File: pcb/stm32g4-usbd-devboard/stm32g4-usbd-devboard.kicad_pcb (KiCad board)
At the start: 2 copper layers, 23.1 x 51.9 mm, 30 parts, among them J1 USB_B_Mini, J2 PIN H 6P, J3 LEFT, J4 RIGHT, U1 USBLC6-2SC6, U2 MCP1700-3302E, U3 STM32G431KBTx, Y1 24MHz

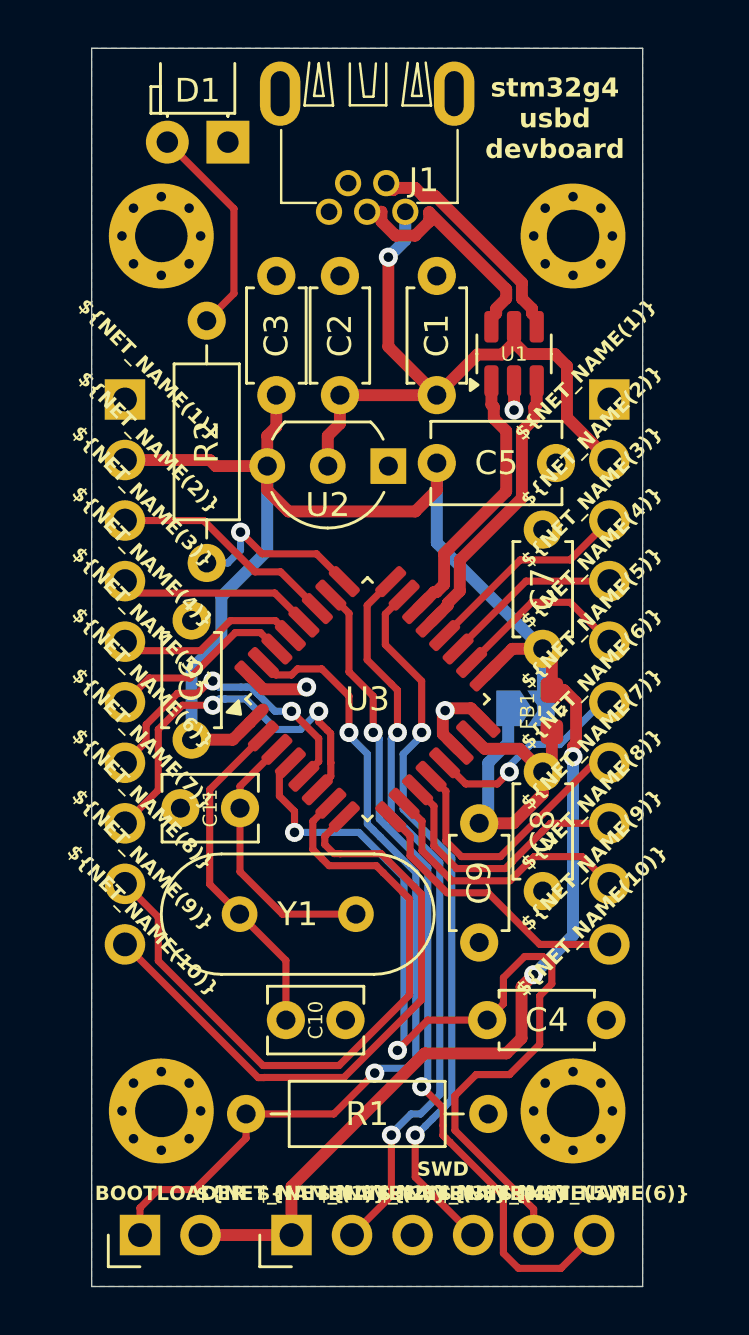
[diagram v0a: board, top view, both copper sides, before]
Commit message: pcb: *: new revision: 20250412
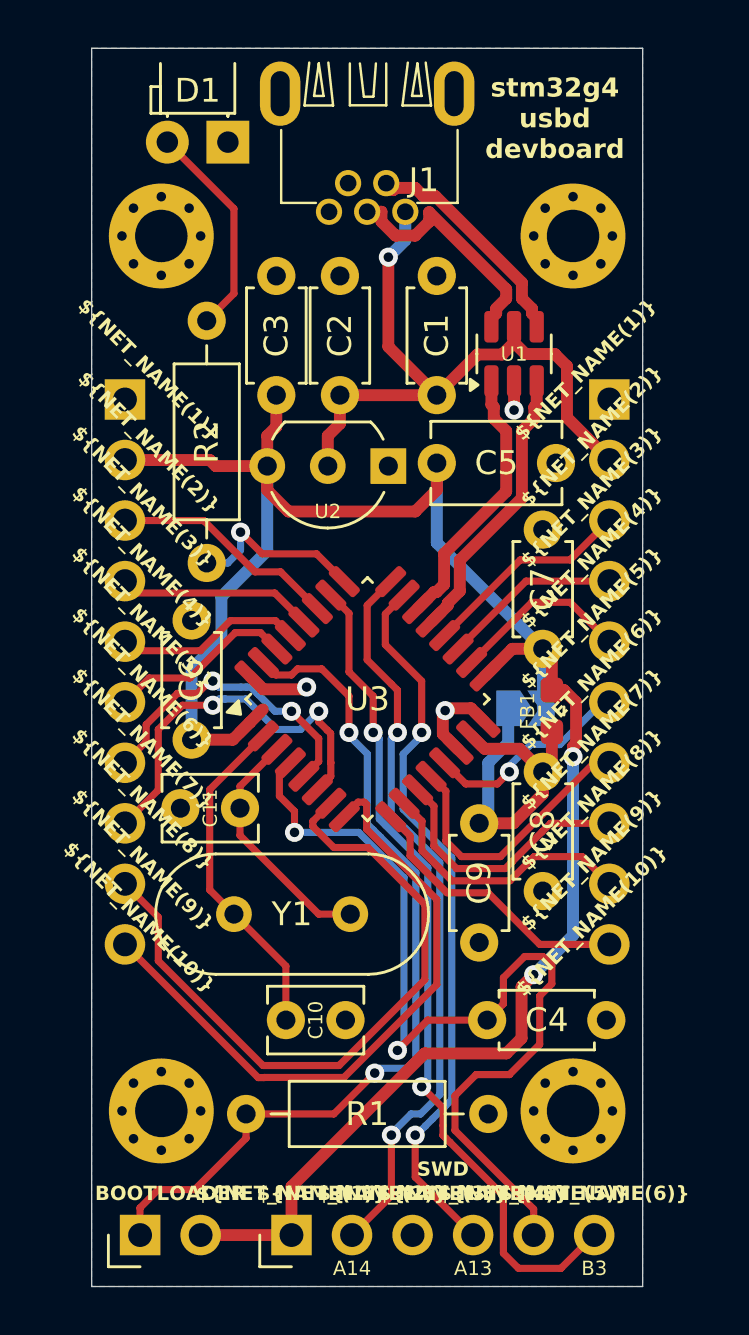
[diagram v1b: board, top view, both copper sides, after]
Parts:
- removed JP2: BOOTLOADER, custom:PinHeader_Bootloader_1x02_P2.54mm_Horizontal
- added J5: BOOTLOADER, custom:PinHeader_Bootloader_1x02_P2.54mm_Horizontal, F.Cu at (137.5, 128.1)
- moved Y1 0.24 mm to (146.4, 114.7)
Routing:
- net F1: track 11.4 -> 10.2 mm

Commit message: pcb: g4: upgrade to kicad 10
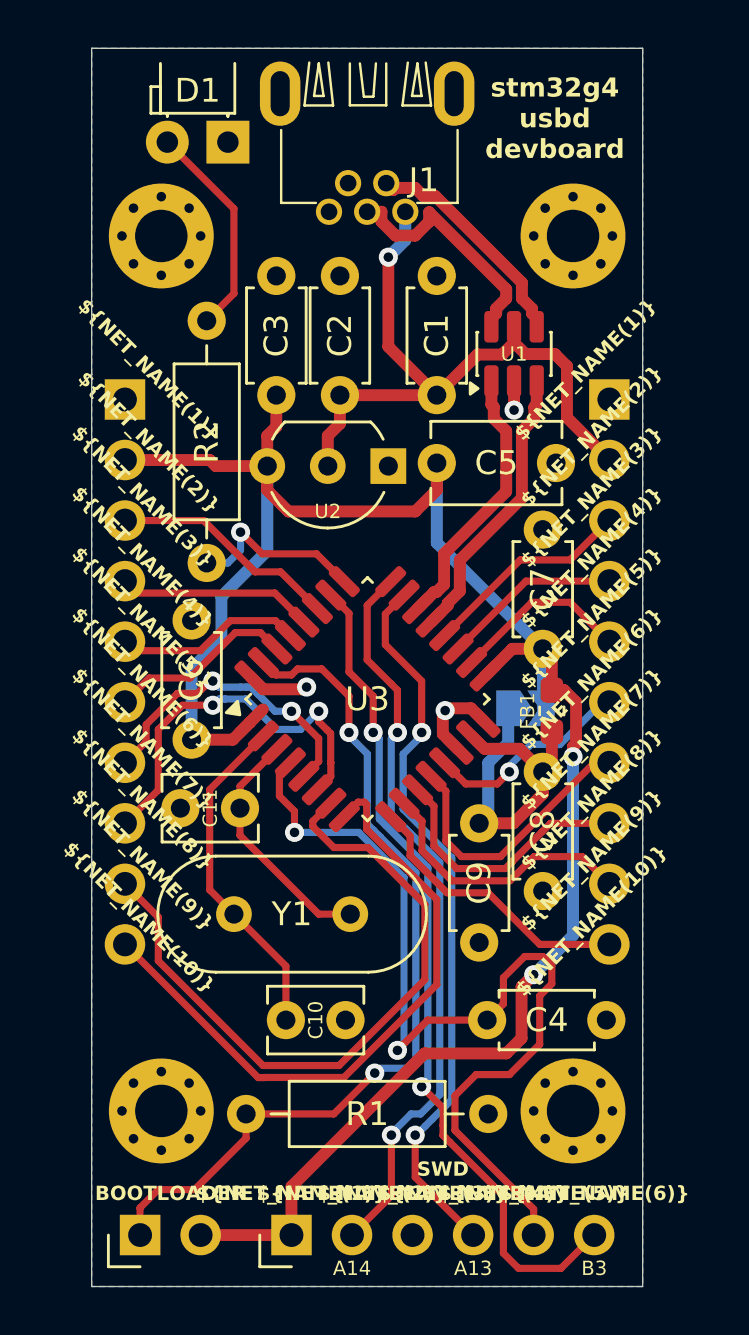
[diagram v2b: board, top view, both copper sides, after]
